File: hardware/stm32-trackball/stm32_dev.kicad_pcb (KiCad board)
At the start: 2 copper layers, 81 x 30.2 mm, 49 parts, among them J1 USB_C_Receptacle_USB2.0, J2 SWD, J3 UART, J4 Spare, J5 Breakout, J6 Breakout, SW1 SIDE, SW2 SIDE, SW3 SW_Push, T1 Trackball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

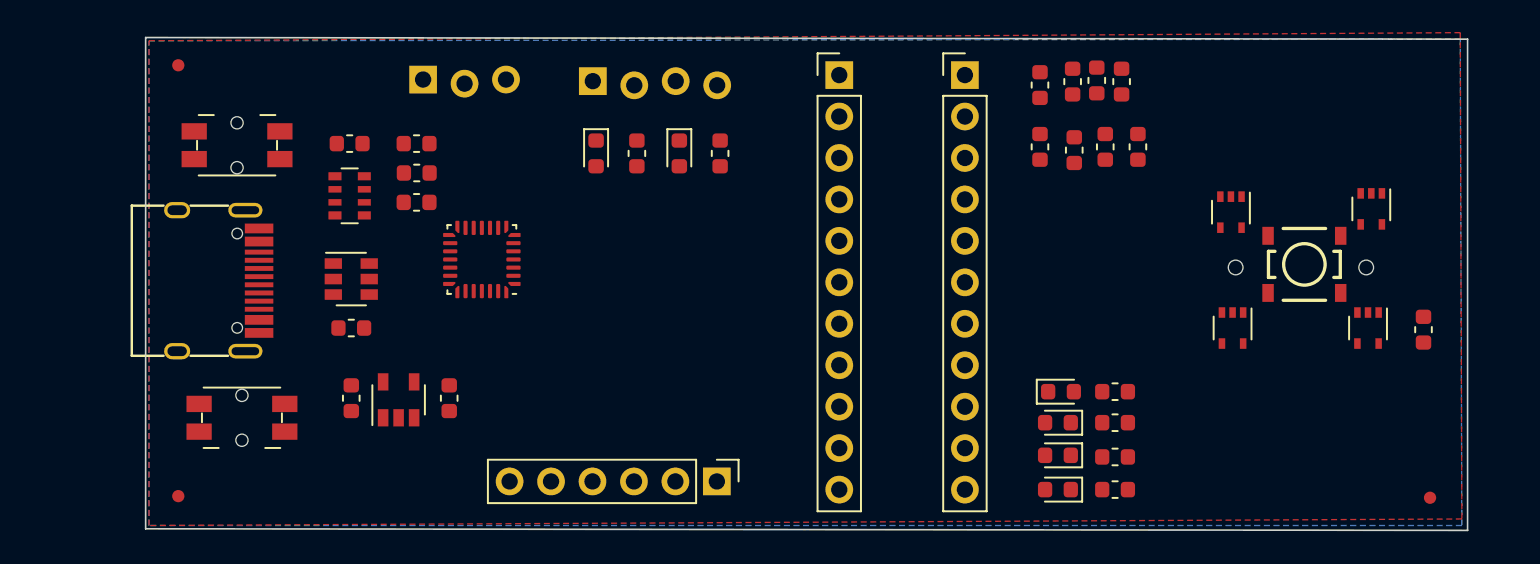
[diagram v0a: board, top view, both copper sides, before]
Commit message: partial layout, trackball TODO
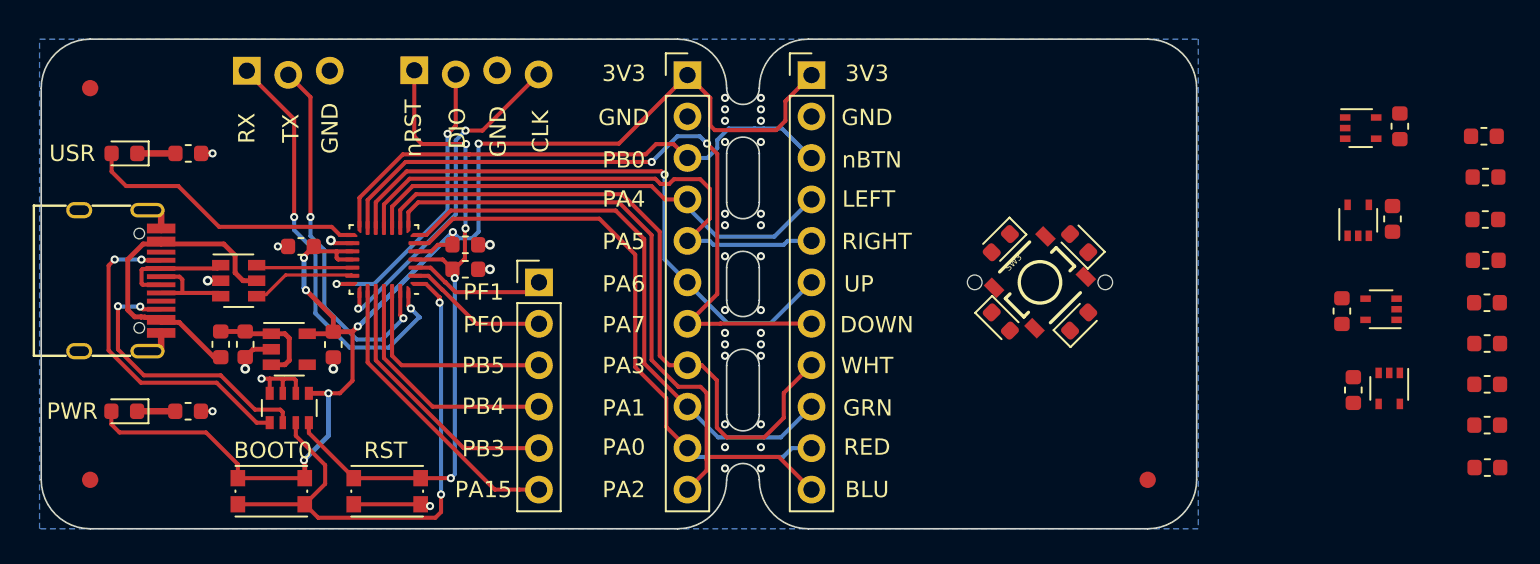
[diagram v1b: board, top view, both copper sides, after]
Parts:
- removed C4: 100n, Capacitor_SMD:C_0603_1608Metric
- removed FID1, FID2, FID3: Fiducial_0.75mm_Mask1.5mm, Fiducial:Fiducial_0.75mm_Mask1.5mm
- added H1: Fuduical, Fiducial:Fiducial_1mm_Mask2mm, F.Cu at (137.8, 113.0)
- added H2: Fuduical, Fiducial:Fiducial_1mm_Mask2mm, F.Cu at (73.0, 89.0)
- added H3: Fuduical, Fiducial:Fiducial_1mm_Mask2mm, F.Cu at (73.0, 113.0)
- J4: value Spare -> SPARE
- SW1, SW2: footprint josh-buttons-switches:Panasonic_EVQPUL_EVQPUC -> josh-buttons-switches:SW_Push_KMR2
- moved D2 37.5 mm to (75.1, 108.8), turned to 180 degrees
- moved R2 36.2 mm to (79.0, 108.8), turned to 0 degrees
- moved R6 29.0 mm to (158.6, 102.2), turned to 180 degrees
- moved D1 28.9 mm to (75.1, 93.0), turned to 180 degrees
- moved R1 27.5 mm to (79.0, 93.0), turned to 0 degrees
- moved R5 26.1 mm to (158.5, 99.5), turned to 180 degrees
- moved C7 25.6 mm to (150.4, 107.5), turned to 90 degrees
- moved R4 23.7 mm to (158.5, 97.0), turned to 180 degrees
- moved R10 23.0 mm to (158.6, 104.7), turned to 180 degrees
- moved R9 22.9 mm to (158.6, 107.2)
- moved R8 22.9 mm to (158.6, 109.7)
- moved R7 22.9 mm to (158.6, 112.2), turned to 180 degrees
- moved C9 22.2 mm to (153.2, 91.3), turned to 90 degrees
- moved R3 21.4 mm to (158.5, 94.5), turned to 180 degrees
- moved SW1 21.3 mm to (84.1, 113.7), turned to 180 degrees
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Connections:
- net /USB_DM renamed /USB_N
- net /USB_DP renamed /USB_P
- J4 pad 6: (no net) -> /SPARE_6
- U3 pad 2: /SPARE_1 -> /SPARE_2
- U3 pad 23: /SPARE_5 -> /SPARE_6
- U3 pad 24: /SPARE_3 -> /SPARE_5
- U3 pad 26: /SPARE_5 -> /SPARE_3
- U3 pad 3: /SPARE_2 -> /SPARE_1
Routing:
- net +3V3: track 0.00 -> 85.1 mm, vias 0 -> 7
- net /TB_DOWN: track 0.00 -> 44.0 mm, vias 0 -> 2
- net /nLED_BLU: track 0.00 -> 42.5 mm
- net /nLED_WHT: track 0.00 -> 41.7 mm
- net /nRST: track 0.00 -> 41.5 mm, vias 0 -> 4
- net /TB_UP: track 0.00 -> 37.0 mm, vias 0 -> 1
- net /nLED_RED: track 0.00 -> 36.2 mm
- net /nLED_GRN: track 0.00 -> 35.8 mm
- net /BOOT0: track 0.00 -> 34.2 mm, vias 0 -> 2
- net /TB_RIGHT: track 0.00 -> 34.1 mm
- net /nTB_BUTTON: track 0.00 -> 33.1 mm
- net /TB_LEFT: track 0.00 -> 30.0 mm
- net /UART_RX: track 0.00 -> 26.5 mm, vias 0 -> 2
- net /UART_TX: track 0.00 -> 23.1 mm, vias 0 -> 2
- net GND: track 0.00 -> 22.6 mm, vias 0 -> 23
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- removed copper zone on F.Cu, net +3V3
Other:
- board size 81 x 30.2 mm -> 70.8 x 30 mm
- board text added: "3V3"
- board text added: "BLU"
- board text added: "BOOT0"
- board text added: "CLK"
- board text added: "DIO"
- board text added: "DOWN"
- board text added: "GND"
- board text added: "GRN"
- board text added: "LEFT"
- board text added: "PA0"
- board text added: "PA1"
- board text added: "PA15"
- board text added: "PA2"
- board text added: "PA3"
- board text added: "PA4"
- board text added: "PA5"
- board text added: "PA6"
- board text added: "PA7"
- board text added: "PB0"
- board text added: "PB3"
- board text added: "PB4"
- board text added: "PB5"
- board text added: "PF0"
- board text added: "PF1"
- board text added: "PWR"
- board text added: "RED"
- board text added: "RIGHT"
- board text added: "RST"
- board text added: "RX"
- board text added: "TX"
- board text added: "UP"
- board text added: "USR"
- board text added: "WHT"
- board text added: "nBTN"
- board text added: "nRST"
- board text removed: "Option to snap breakout off"

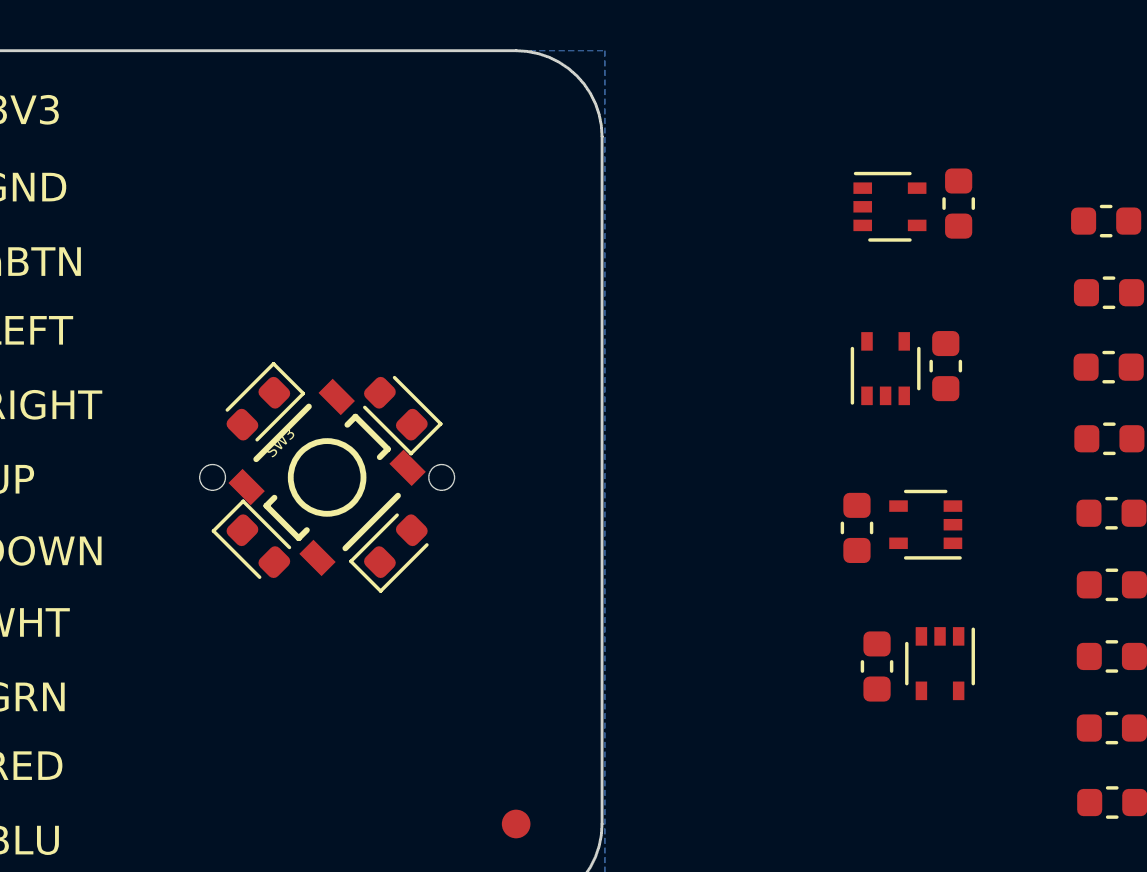
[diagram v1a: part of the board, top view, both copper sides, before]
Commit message: fix trackball led / hall position
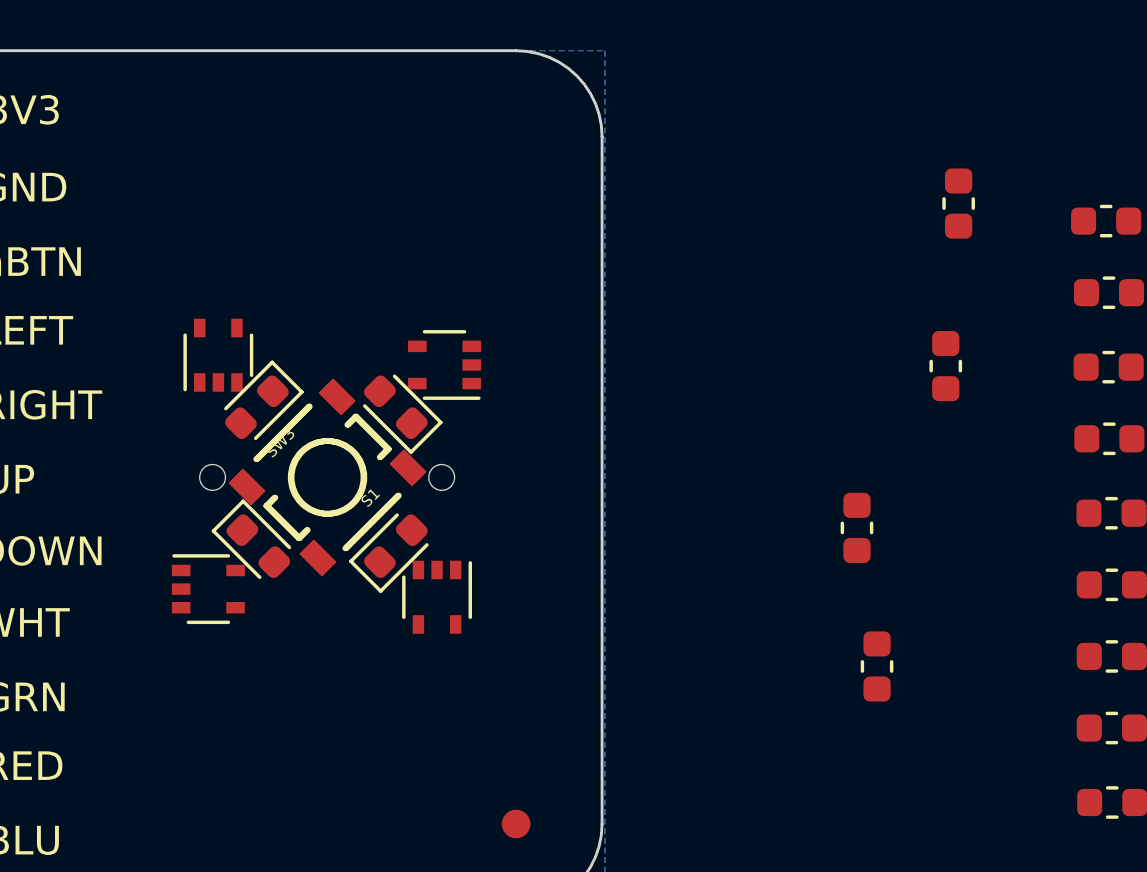
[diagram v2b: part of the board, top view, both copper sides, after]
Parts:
- added FRAME1: FRAME-LETTER, SparkFun_Blackberry_Trackballer_Breakout_v13:CREATIVE_COMMONS, F.Cu at (191.7, 136.3)
- added FRAME1: FRAME-LETTER, SparkFun_Blackberry_Trackballer_Breakout_v13:CREATIVE_COMMONS, F.Cu at (191.8, 136.4)
- added S1: SWITCH-MOMENTARY-2SMD-2, SparkFun_Blackberry_Trackballer_Breakout_v13:TACTILE_SWITCH_SMD-2, F.Cu at (131.2, 100.9)
- moved U7 24.9 mm to (127.1, 104.8), turned to 0 degrees
- moved U4 24.0 mm to (127.4, 96.6), turned to 90 degrees
- moved U5 17.7 mm to (135.0, 105.1)
- moved U6 17.7 mm to (135.3, 97.0)
- moved D5 0.07 mm to (128.8, 98.5)
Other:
- net class Default: via_dia 0.5 -> 0.8; via_drill 0.25 -> 0.4
- rule pad_to_mask_clearance: 0 -> 0.05
- rule trace_min: 0.15 -> 0.2
- rule via_min_drill: 0.25 -> 0.3
- rule via_min_size: 0.5 -> 0.4
- board text added: "Nathan Seidle"
- board text added: "Revised by: Patrick Alberts"

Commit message: test
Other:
- board text removed: "Nathan Seidle"
- board text removed: "Revised by: Patrick Alberts"

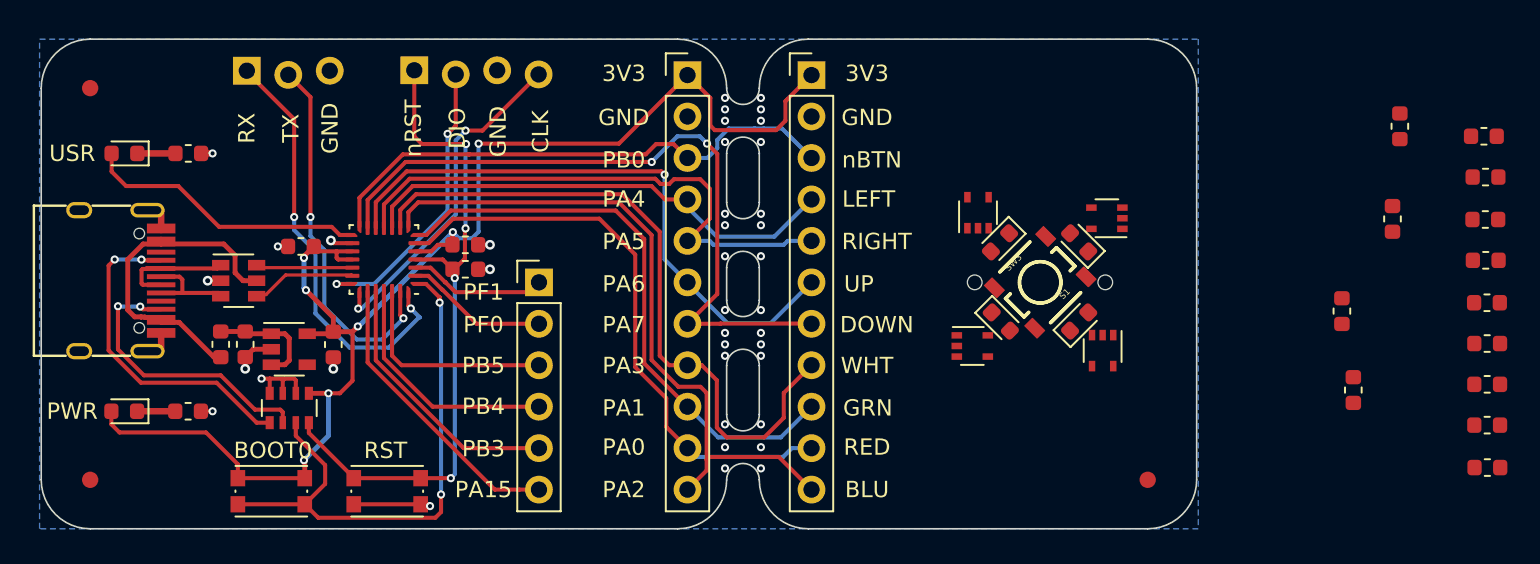
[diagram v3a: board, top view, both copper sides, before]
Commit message: Trackball breakout mounting holes and almost-finished routing
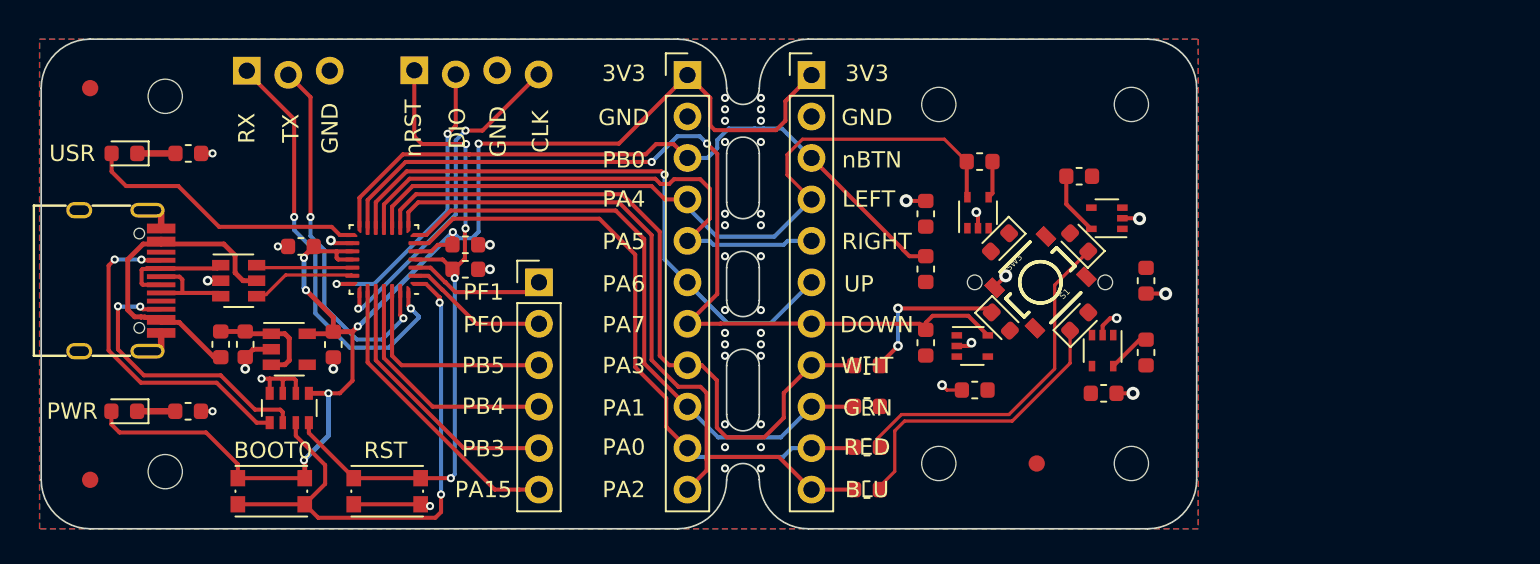
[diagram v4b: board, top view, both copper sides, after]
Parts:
- added REF**: MountingHole_2.1mm, MountingHole:MountingHole_2.1mm, F.Cu at (77.6, 89.5)
- added REF**: MountingHole_2.1mm, MountingHole:MountingHole_2.1mm, F.Cu at (77.6, 112.5)
- added REF**: MountingHole_2.1mm, MountingHole:MountingHole_2.1mm, F.Cu at (136.8, 90.0)
- added REF**: MountingHole_2.1mm, MountingHole:MountingHole_2.1mm, F.Cu at (125.0, 90.0)
- added REF**: MountingHole_2.1mm, MountingHole:MountingHole_2.1mm, F.Cu at (136.8, 112.0)
- added REF**: MountingHole_2.1mm, MountingHole:MountingHole_2.1mm, F.Cu at (125.0, 112.0)
- H1, H2, H3: value Fuduical -> Fiducial
- moved R7 38.0 mm to (120.6, 113.6)
- moved R10 38.0 mm to (120.6, 106.0)
- moved R8 38.0 mm to (120.6, 111.0)
- moved R9 38.0 mm to (120.6, 108.5)
- moved R11 35.2 mm to (124.2, 100.1), turned to 90 degrees
- moved R6 34.5 mm to (124.2, 104.6), turned to 90 degrees
- moved R3 31.0 mm to (127.5, 93.5)
- moved C9 29.5 mm to (124.2, 96.7)
- moved R5 25.4 mm to (133.6, 94.4)
- moved C8 23.0 mm to (127.2, 107.5), turned to 180 degrees
- moved R4 22.3 mm to (137.7, 105.2), turned to 90 degrees
- moved C10 15.6 mm to (137.7, 100.8)
- moved C7 15.3 mm to (135.1, 107.7), turned to 0 degrees
- moved H1 6.87 mm to (131.0, 112.0)
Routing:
- net Net-(D4-Pad1): track 0.00 -> 21.2 mm
- net Net-(D3-Pad1): track 0.00 -> 18.8 mm
- net /TB_LEFT: track 30.0 -> 47.6 mm
- net /TB_DOWN: track 44.0 -> 56.0 mm
- net GND: track 22.6 -> 33.1 mm, vias 23 -> 32
- net Net-(D6-Pad1): track 0.00 -> 9.97 mm, vias 0 -> 2
- net /nTB_BUTTON: track 33.1 -> 42.6 mm
- net /TB_UP: track 37.0 -> 40.9 mm
- net /TB_RIGHT: track 34.1 -> 36.8 mm
- net /nLED_RED: track 36.2 -> 38.7 mm
- net /nLED_BLU: track 42.5 -> 44.9 mm
- net /nLED_WHT: track 41.7 -> 44.2 mm
- net /nLED_GRN: track 35.8 -> 38.2 mm
- net +3V3: track 85.1 -> 87.4 mm
- added copper zone on F.Cu, net +3V3

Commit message: Flipped TB_UP and TB_RIGHT for more convenient routing on the trackball. Almost finished routing, pad-on-pad issues with the Switch and Trackball footprints prevent routing GNDs
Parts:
- H1, H2, H3: value Fiducial -> Fuduical
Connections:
- J1 pad A8: (no net) -> Net-(J1-PadA8)
- J1 pad B8: (no net) -> Net-(J1-PadB8)
- J5 pad 5: /TB_RIGHT -> /TB_UP
- J5 pad 6: /TB_UP -> /TB_RIGHT
- J6 pad 5: /TB_RIGHT -> /TB_UP
- J6 pad 6: /TB_UP -> /TB_RIGHT
- U1 pad 4: (no net) -> Net-(U1-Pad4)
- U3 pad 11: /TB_RIGHT -> /TB_UP
- U3 pad 12: /TB_UP -> /TB_RIGHT
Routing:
- net /TB_RIGHT: track 36.8 -> 66.8 mm, vias 0 -> 3
- net Net-(D5-Pad1): track 0.00 -> 18.5 mm, vias 0 -> 2
- net /TB_UP: track 40.9 -> 55.6 mm

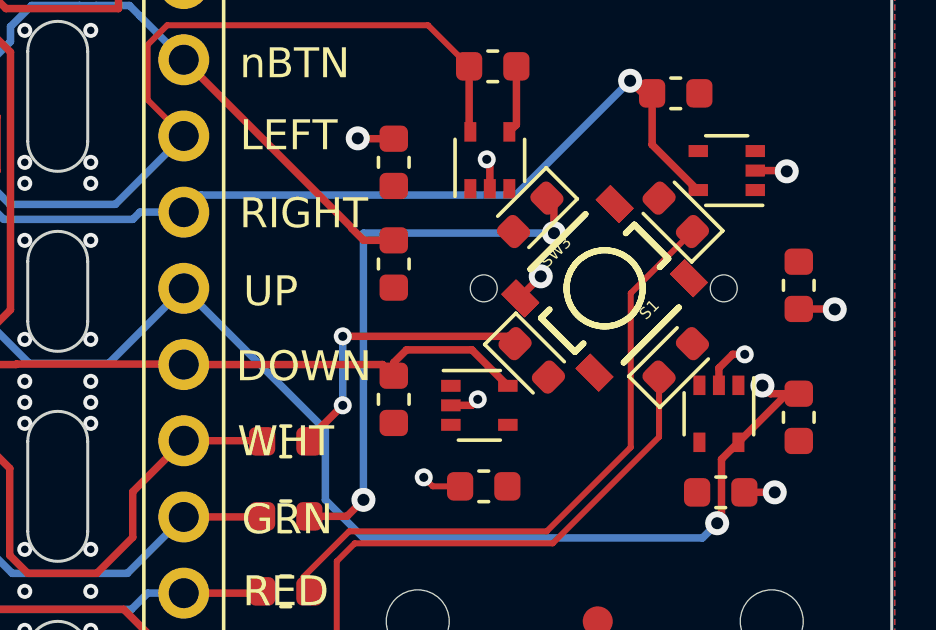
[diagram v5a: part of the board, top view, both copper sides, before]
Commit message: Removed S1 in favour of SW3, first pass (naive) routing finished
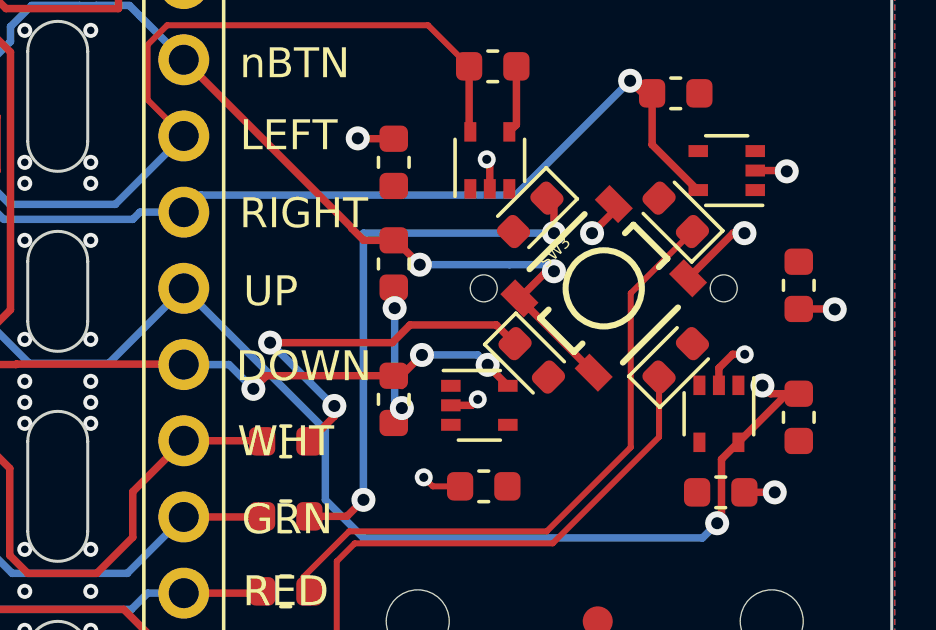
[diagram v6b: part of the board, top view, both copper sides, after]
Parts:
- removed S1: SWITCH-MOMENTARY-2SMD-2, SparkFun_Blackberry_Trackballer_Breakout_v13:TACTILE_SWITCH_SMD-2
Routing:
- net /nTB_BUTTON: track 42.6 -> 53.9 mm, vias 0 -> 2
- net +3V3: track 87.4 -> 92.1 mm, vias 7 -> 9
- net Net-(D6-Pad1): track 9.97 -> 13.3 mm
- net GND: track 33.1 -> 35.8 mm, vias 32 -> 33
- net /TB_DOWN: track 56.0 -> 56.5 mm, vias 2 -> 5
